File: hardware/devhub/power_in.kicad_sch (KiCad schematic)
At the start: 31 parts, among them J1 USB-C PWR IN, U1 AP7361C-33E, U13 TPS259470ARPWR

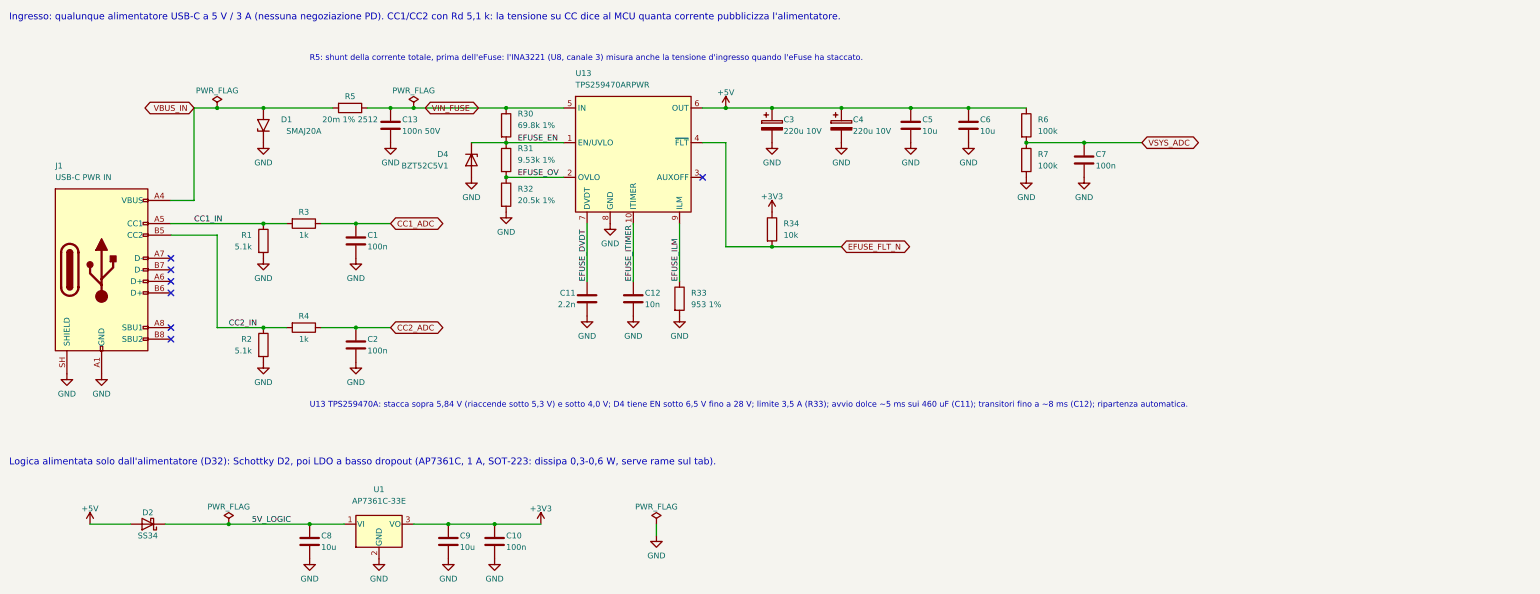
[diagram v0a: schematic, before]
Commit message: Simplification: input shunt moved after the eFuse, VSYS_ADC divider removed (D40)
The INA3221 is no longer exposed to the supply voltage and reads 5V_SYS; LOCAL_PWR gets a 10k pull-up (R26). Push-button capacitors kept (D39).
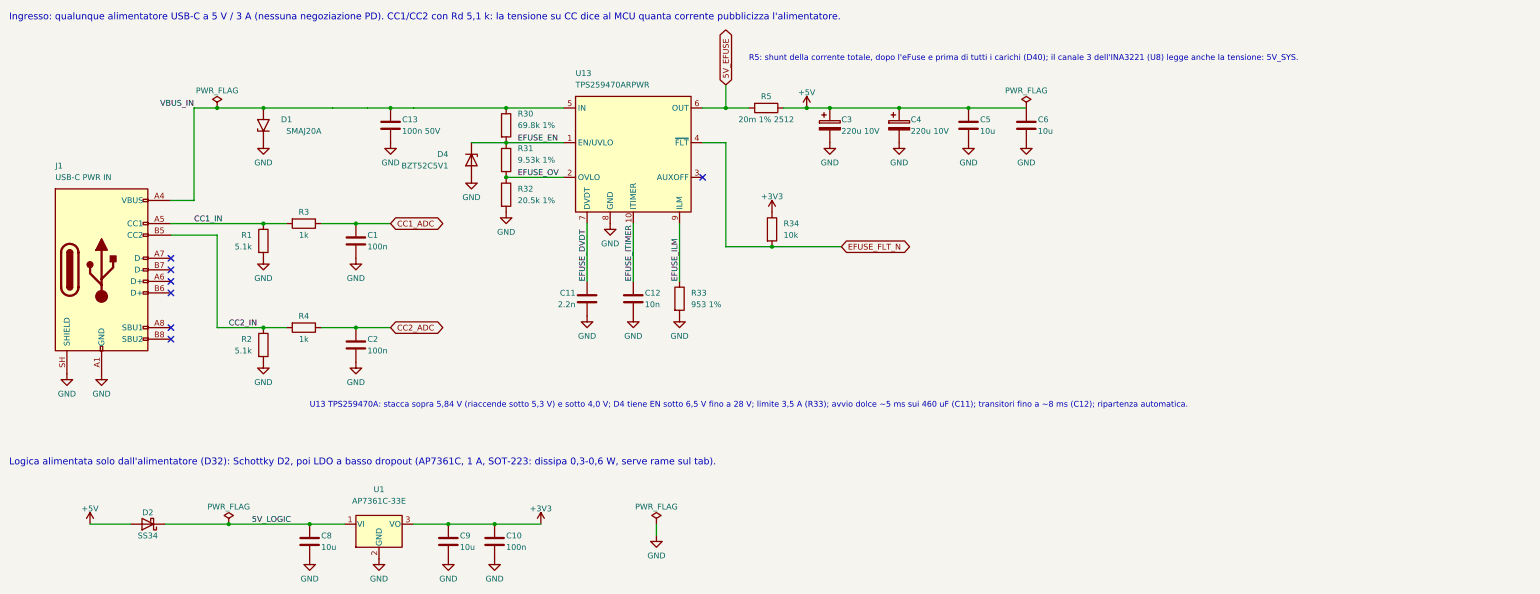
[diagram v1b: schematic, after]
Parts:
- removed C7: 100n, Capacitor_SMD:C_0603_1608Metric, symbol Device:C
- removed R6, R7: 100k, Resistor_SMD:R_0603_1608Metric, symbol Device:R
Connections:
- net +5V: now also R5.1; no longer U13.6 (OUT)
- net VBUS_IN: now also C13.1, R30.1, U13.5 (IN); no longer R5.2
- removed net VIN_FUSE: C13.1, R30.1, R5.1, U13.5 (IN)
- new net 5V_EFUSE: R5.2, U13.6 (OUT)
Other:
- note added: "R5: shunt della corrente totale, dopo l'eFuse e prima di tutti i carichi (D40); il canale 3 dell'INA3221 (U8) legge anche la tensione: 5V_SYS."
- note removed: "R5: shunt della corrente totale, prima dell'eFuse: l'INA3221 (U8, canale 3) misura anche la tensione d'ingresso quando l'eFuse ha staccato."
- moved on the sheet: C3, C4, C5, C6, R5

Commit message: Intial PCB layout
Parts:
- U13: footprint (none) -> lcsc_footprints:C3662799_VQFN-10_L2_0-W2_0-P0_45-TL

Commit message: PCB rules in KiCad, USB pair names, eFuse output bypass and U2 thermal vias (D44-D50)
Stackup JLC04161H-7628, netclasses and custom DRC rules (devhub.kicad_dru) from
docs/regole-pcb.md, with a section for the checks that DRC cannot cover. C7 1 uF on
the TPS259470A output before the shunt (D48). USB nets renamed to DP/DN so KiCad
recognizes the differential pairs (D49). U2 footprint with 0.3 mm thermal vias, open
on both sides for the prototype; encroached vias and a JLCPCB order note for
production (D50). Also includes stock part codes, cost comparison and placement rules
(D44-D47).
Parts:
- added C7: 1u 25V, Capacitor_SMD:C_0603_1608Metric, symbol Device:C
- C1, C10, C13, C2: digikey (none) -> 1276-1000-1-ND; lcsc (none) -> C1591; mouser (none) -> 187-CL10B104KB8NNNC; warehouse (none) -> 235
- C11: digikey (none) -> 1276-1110-1-ND; lcsc (none) -> C16033; mouser (none) -> 187-CL10B222KB8NNNC
- C12: digikey (none) -> 1276-1009-1-ND; lcsc (none) -> C1589; mouser (none) -> 187-CL10B103KB8NNNC; warehouse (none) -> 234
- C3, C4: footprint Capacitor_THT:CP_Radial_D8.0mm_P3.50mm -> Capacitor_THT:CP_Radial_D6.3mm_P2.50mm; digikey (none) -> P14375-ND; lcsc (none) -> C238354; mouser (none) -> 667-EEU-FR1A221; warehouse (none) -> 60
- C5, C6, C8, C9: digikey (none) -> 490-18663-1-ND; lcsc (none) -> C440198; mouser (none) -> 81-GRM21BR61H106KE3L; warehouse (none) -> 192
- D1: digikey (none) -> SMAJ20A-FDICT-ND; lcsc (none) -> C134969; mouser (none) -> 621-SMAJ20A-13-F; warehouse (none) -> 221
- D2: digikey (none) -> B340A-FDICT-ND; lcsc (none) -> C85098; mouser (none) -> 621-B340A-F
- D4: digikey (none) -> BZT52C5V1-FDICT-ND; lcsc (none) -> C151588; mouser (none) -> 621-BZT52C5V1-F
- J1: digikey (none) -> 2073-USB4105-GF-ACT-ND; lcsc (none) -> C3020560; mouser (none) -> 640-USB4105-GF-A; warehouse (none) -> 279
- R1, R2: digikey (none) -> 311-5.10KHRCT-ND; lcsc (none) -> C23186; mouser (none) -> 603-RC0603FR-075K1L; warehouse (none) -> 238
- R3, R4: digikey (none) -> 311-1.00KHRCT-ND; lcsc (none) -> C21190; mouser (none) -> 603-RC0603FR-071KL; warehouse (none) -> 284
- R30: digikey (none) -> 311-69.8KHRCT-ND; lcsc (none) -> C137689; mouser (none) -> 603-RC0603FR-0769K8L
- R31: digikey (none) -> 311-9.53KHRCT-ND; lcsc (none) -> C23127; mouser (none) -> 603-RC0603FR-079K53L
- R32: digikey (none) -> 311-20.5KHRCT-ND; lcsc (none) -> C273789; mouser (none) -> 603-RC0603FR-0720K5L
- R33: digikey (none) -> 311-953HRCT-ND; lcsc (none) -> C137668; mouser (none) -> 603-RC0603FR-07953RL
- R34: digikey (none) -> 311-10.0KHRCT-ND; lcsc (none) -> C2906982; mouser (none) -> 603-RC0603FR-0710KL; warehouse (none) -> 248
- R5: digikey (none) -> 311-0.02TCT-ND; lcsc (none) -> C326611; mouser (none) -> 603-RL2512FK-070R02L
- U1: digikey (none) -> AP7361C-33E-13DICT-ND; lcsc (none) -> C500795; mouser (none) -> 621-AP7361C-33E-13
- U13: digikey (none) -> 296-TPS259470ARPWRCT-ND; lcsc (none) -> C3662799; mouser (none) -> 595-TPS259470ARPWR
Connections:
- net 5V_EFUSE: now also C7.1
- net GND: now also C7.2
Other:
- moved on the sheet: R5

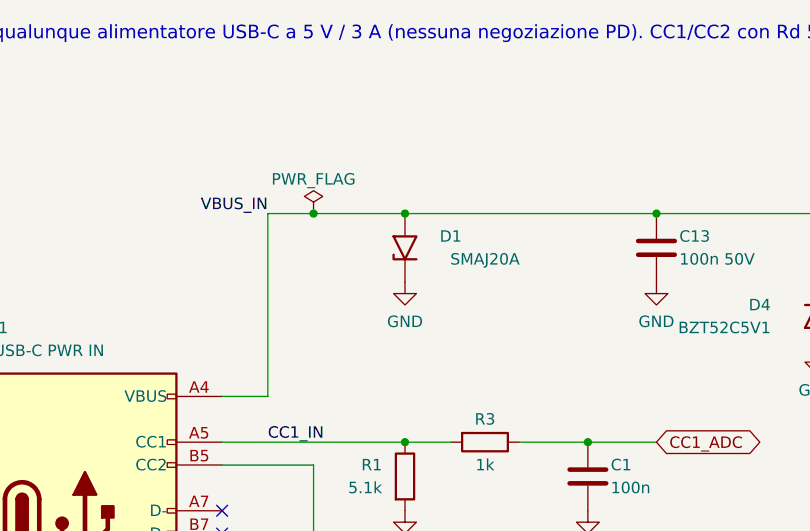
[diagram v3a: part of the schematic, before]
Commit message: Review 03 fixes and PCB placement update (D51-D56)
Schematic review 03 (docs/lavorazioni/review_03.md):
- D1 SMAJ20A was reversed (cathode on GND): rotated, and replaced by a project
  symbol devhub:SMAJ20A with explicit K/A pin names; breakdown corrected to
  22.2-24.5 V (R03-01).
- D21 BAT54WS from VBUS_DET to 3V3 keeps USB2517 pin 44 within VDD33 + 0.5 V
  when the hub is unpowered (D53, R03-02).
- USB-A port limited to 1.5 A, the J501 connector rating: R62 33.2k, RF-5
  updated (D54, R03-03).
- RF-6 accuracy relaxed to 2 mA + 5 % because of the thick-film shunt TCR
  (D55, R03-04).
- Courtyards of the LCSC U13 and PI3USB4002A footprints enlarged to cover the
  pads, also in the PCB copies (R03-05).
- LDO U1 kept (buck rejected); GND heatsink zone and 10 vias on its tab, thermal
  budget corrected to 0.8-0.9 W worst case (D56).

PCB: connector layout (D51), USB pair polarity on the bottom side (D52), relays
moved with the contact keepout areas redrawn, D21 placed next to C21. Cost
comparison updated with D21 and R62.
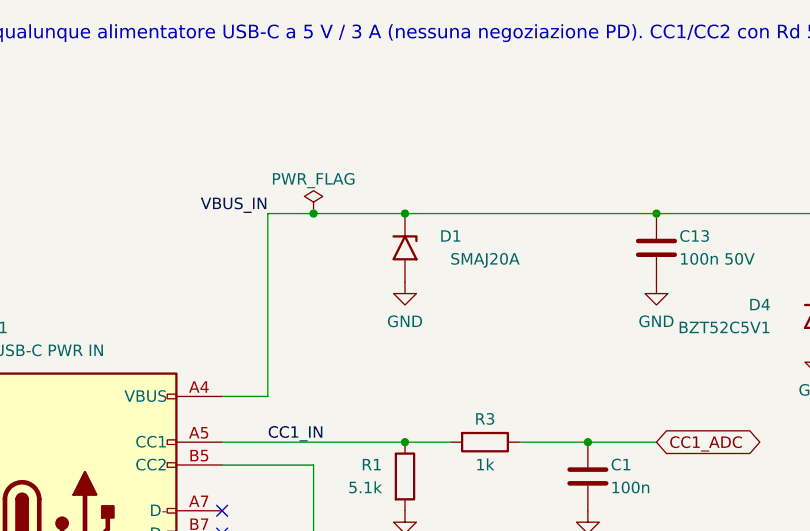
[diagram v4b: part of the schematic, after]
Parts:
- D1: symbol Diode:SMAJ20A -> devhub:SMAJ20A
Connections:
- net GND: now also D1.2 (A); no longer D1.1 (A1)
- net VBUS_IN: now also D1.1 (K); no longer D1.2 (A2)
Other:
- moved on the sheet: D1
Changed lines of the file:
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@@
 	)
 	(symbol
-		(lib_id "Diode:SMAJ20A")
-		(at 66.04 39.37 90)
+		(lib_id "devhub:SMAJ20A")
+		(at 66.04 39.37 270)
 		(unit 1)
 		(body_style 1)

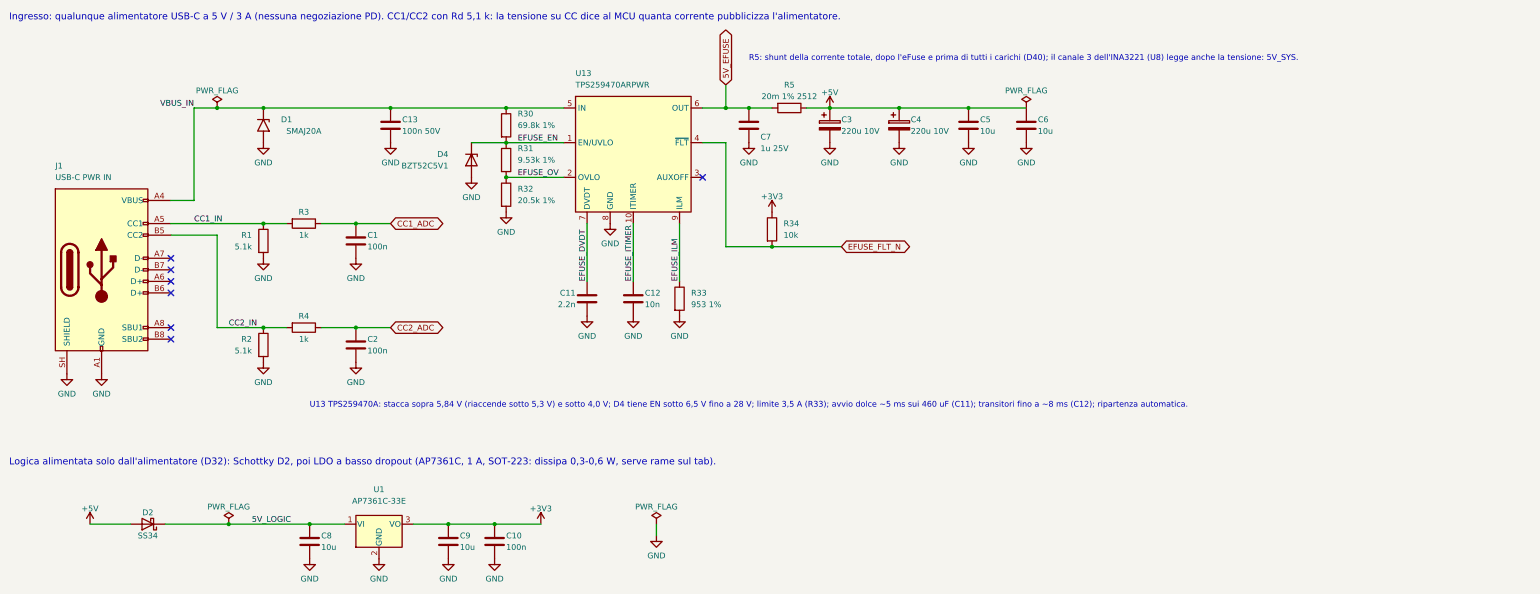
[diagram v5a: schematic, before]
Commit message: Schematic v0.3: apply simplified requirements (D79-D81)
Update the existing KiCad project instead of starting over:
- MCU U3 replaced with STM32G0B1CEU6 (UFQFPN48) on the 48-pin pinout
- switches sheet: two UCS2114-1-V/LX on separate I2C buses replace
  TPS2561A, INA3221 and current shunts
- ports: single MCU-driven LED, discrete VBUS discharge removed
- remove USB-A port, spare hub header, second relay channel,
  input CC ADC filters and input shunt
- add UCS2114 symbol and footprint (Microchip land pattern C04-2421)
- align pinout, decisions, architecture and component docs
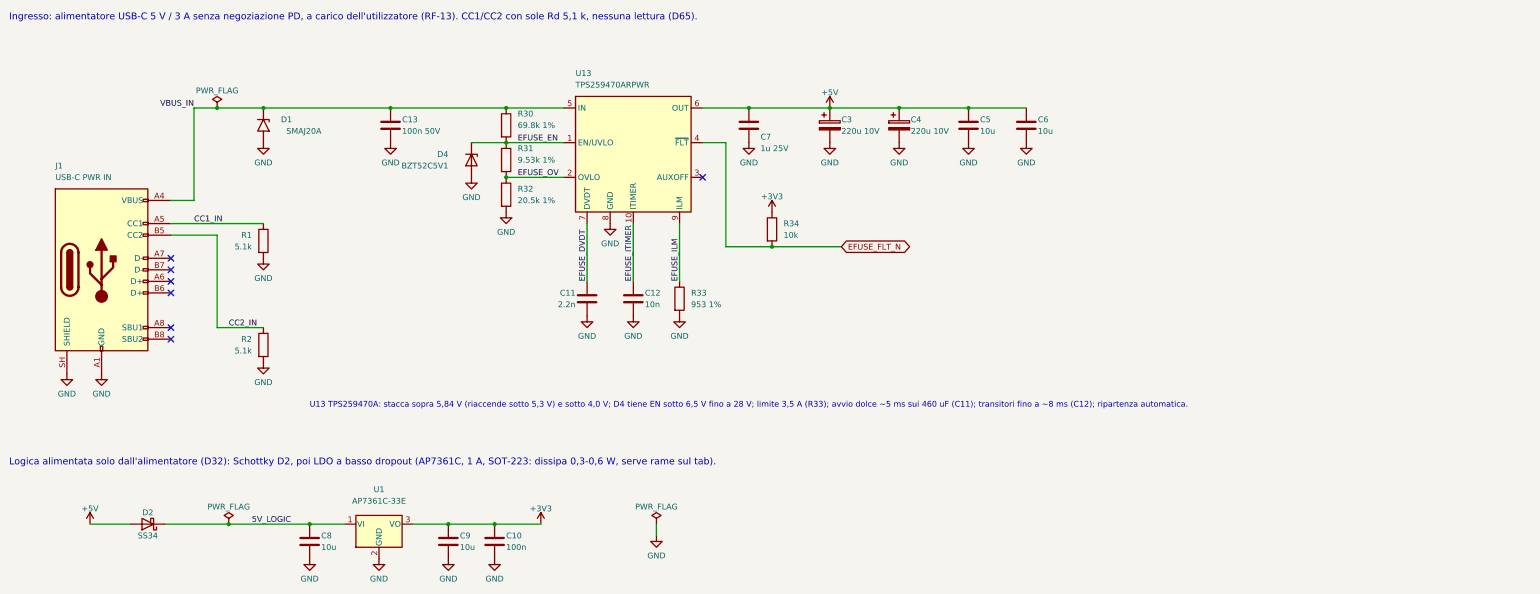
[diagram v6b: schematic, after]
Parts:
- removed C1, C2: 100n, Capacitor_SMD:C_0603_1608Metric, symbol Device:C
- removed R3, R4: 1k, Resistor_SMD:R_0603_1608Metric, symbol Device:R
- removed R5: 20m 1% 2512, Resistor_SMD:R_2512_6332Metric, symbol Device:R
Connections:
- net 5V_EFUSE is gone; now on net +5V: C7.1, U13.6 (OUT)
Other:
- note added: "Ingresso: alimentatore USB-C 5 V / 3 A senza negoziazione PD, a carico dell'utilizzatore (RF-13). CC1/CC2 con sole Rd 5,1 k, nessuna lettura (D65)."
- note removed: "Ingresso: qualunque alimentatore USB-C a 5 V / 3 A (nessuna negoziazione PD). CC1/CC2 con Rd 5,1 k: la tensione su CC dice al MCU quanta corrente pubblicizza l'alimentatore."
- note removed: "R5: shunt della corrente totale, dopo l'eFuse e prima di tutti i carichi (D40); il canale 3 dell'INA3221 (U8) legge anche la tensione: 5V_SYS."

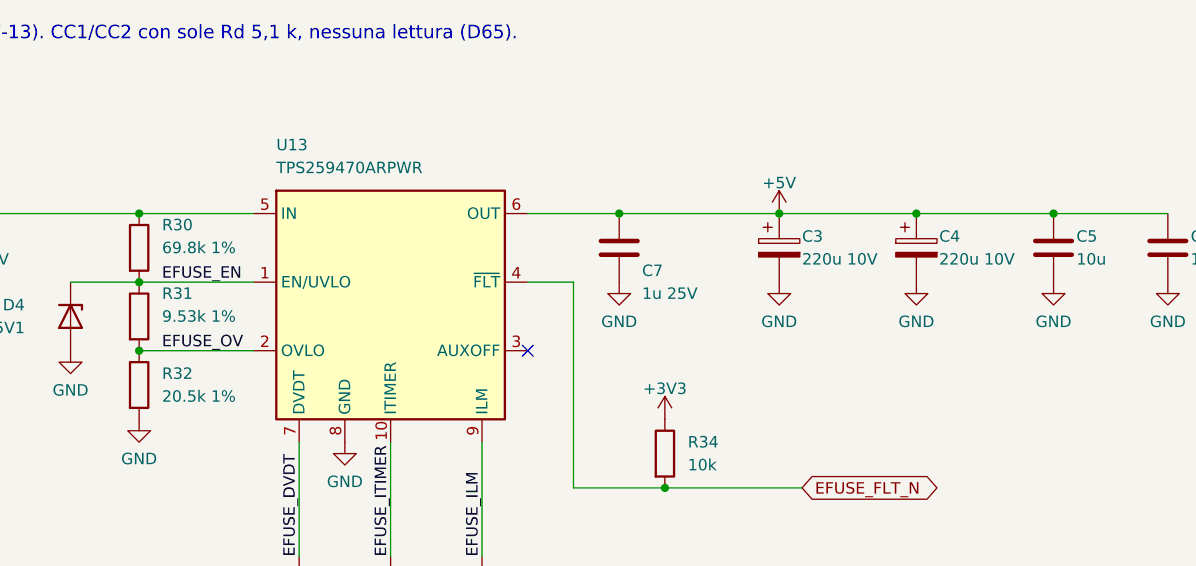
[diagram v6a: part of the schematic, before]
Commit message: Power stage: lower eFuse OVLO, SMD bulk caps, move button row (D85-D87)
- R30/R31 68.1k/8.66k: OVLO 5.52-5.90 V, below the 6 V abs max of UCS2114
- C3/C4 Panasonic EEE-FK1C221XP SMD 220 uF 16 V replace THT radials
- Buttons at v = 14.5 mm from the front edge
- Update power budget and LDO dissipation for four ports
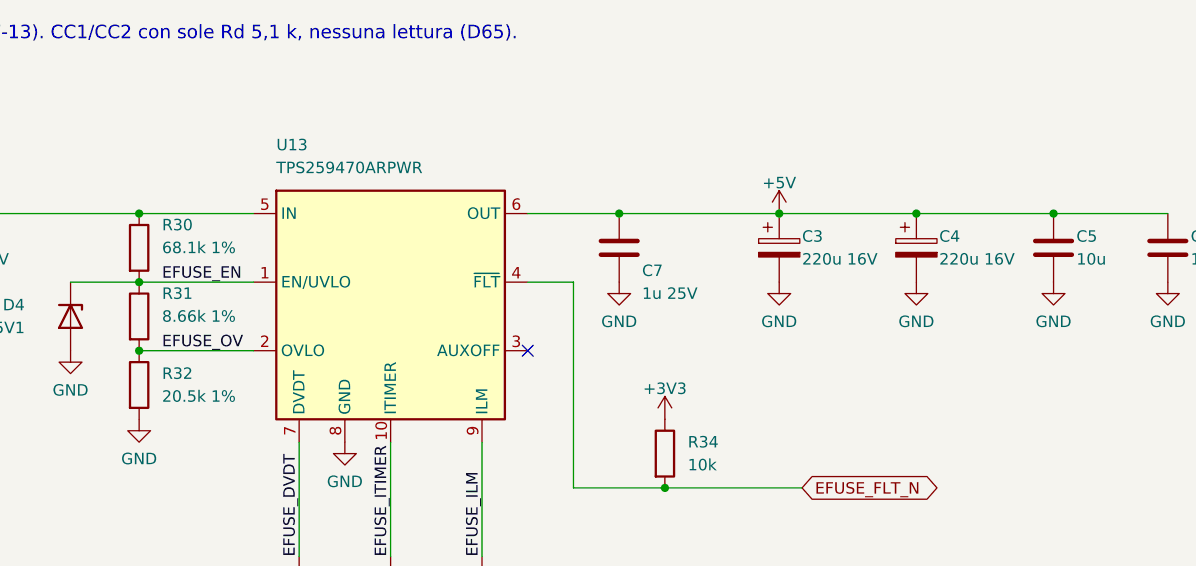
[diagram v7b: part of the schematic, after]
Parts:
- C3, C4: value 220u 10V -> 220u 16V; footprint Capacitor_THT:CP_Radial_D6.3mm_P2.50mm -> Capacitor_SMD:CP_Elec_6.3x7.7; digikey P14375-ND -> PCE3788CT-ND; lcsc C238354 -> C128533; mouser 667-EEU-FR1A221 -> 667-EEE-FK1C221XP; warehouse 60 -> (none)
- R30: value 69.8k 1% -> 68.1k 1%; digikey 311-69.8KHRCT-ND -> 311-68.1KHRCT-ND; lcsc C137689 -> C185315; mouser 603-RC0603FR-0769K8L -> 603-RC0603FR-0768K1L
- R31: value 9.53k 1% -> 8.66k 1%; digikey 311-9.53KHRCT-ND -> 311-8.66KHRCT-ND; lcsc C23127 -> C23114; mouser 603-RC0603FR-079K53L -> 603-RC0603FR-078K66L
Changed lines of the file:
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@@
 			)
 		)
-		(property "Value" "69.8k 1%"
+		(property "Value" "68.1k 1%"
 			(at 121.92 39.37 0)
 			(show_name no)
@@
 			)
 		)
-		(property "lcsc" "C137689"
+		(property "lcsc" "C185315"
 			(at 119.38 39.37 0)
 			(hide yes)
@@
 			)
 		)
-		(property "mouser" "603-RC0603FR-0769K8L"
+		(property "mouser" "603-RC0603FR-0768K1L"
 			(at 119.38 39.37 0)
 			(hide yes)
@@
 			)
 		)
-		(property "digikey" "311-69.8KHRCT-ND"
+		(property "digikey" "311-68.1KHRCT-ND"
 			(at 119.38 39.37 0)
 			(hide yes)
@@
 			)
 		)
-		(property "Value" "220u 10V"
+		(property "Value" "220u 16V"
 			(at 193.04 40.64 0)
 			(show_name no)
@@
 			)
 		)
-		(property "Footprint" "Capacitor_THT:CP_Radial_D6.3mm_P2.50mm"
+		(property "Footprint" "Capacitor_SMD:CP_Elec_6.3x7.7"
 			(at 190.5 39.37 0)
 			(hide yes)
@@
 			)
 		)
-		(property "warehouse" "60"
+		(property "warehouse" ""
 			(at 190.5 39.37 0)
 			(hide yes)
@@
 			)
 		)
-		(property "lcsc" "C238354"
+		(property "lcsc" "C128533"
 			(at 190.5 39.37 0)
 			(hide yes)
@@
 			)
 		)
-		(property "mouser" "667-EEU-FR1A221"
+		(property "mouser" "667-EEE-FK1C221XP"
 			(at 190.5 39.37 0)
 			(hide yes)
@@
 			)
 		)
-		(property "digikey" "P14375-ND"
+		(property "digikey" "PCE3788CT-ND"
 			(at 190.5 39.37 0)
 			(hide yes)
@@
 			)
 		)
-		(property "Value" "220u 10V"
+		(property "Value" "220u 16V"
 			(at 208.28 40.64 0)
 			(show_name no)
@@
 			)
 		)
-		(property "Footprint" "Capacitor_THT:CP_Radial_D6.3mm_P2.50mm"
+		(property "Footprint" "Capacitor_SMD:CP_Elec_6.3x7.7"
 			(at 205.74 39.37 0)
 			(hide yes)
@@
 			)
 		)
-		(property "warehouse" "60"
+		(property "warehouse" ""
 			(at 205.74 39.37 0)
 			(hide yes)
@@
 			)
 		)
-		(property "lcsc" "C238354"
+		(property "lcsc" "C128533"
 			(at 205.74 39.37 0)
 			(hide yes)
@@
 			)
 		)
-		(property "mouser" "667-EEU-FR1A221"
+		(property "mouser" "667-EEE-FK1C221XP"
 			(at 205.74 39.37 0)
 			(hide yes)
@@
 			)
 		)
-		(property "digikey" "P14375-ND"
+		(property "digikey" "PCE3788CT-ND"
 			(at 205.74 39.37 0)
 			(hide yes)
@@
 			)
 		)
-		(property "Value" "9.53k 1%"
+		(property "Value" "8.66k 1%"
 			(at 121.92 46.99 0)
 			(show_name no)
@@
 			)
 		)
-		(property "lcsc" "C23127"
+		(property "lcsc" "C23114"
 			(at 119.38 46.99 0)
 			(hide yes)
@@
 			)
 		)
-		(property "mouser" "603-RC0603FR-079K53L"
+		(property "mouser" "603-RC0603FR-078K66L"
 			(at 119.38 46.99 0)
 			(hide yes)
@@
 			)
 		)
-		(property "digikey" "311-9.53KHRCT-ND"
+		(property "digikey" "311-8.66KHRCT-ND"
 			(at 119.38 46.99 0)
 			(hide yes)
